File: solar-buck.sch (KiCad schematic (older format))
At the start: 52 parts, among them J1 PV_input, J2 Conn_02x19_Odd_Even, J3 Conn_02x19_Odd_Even, J4 Load_output, J5 Batt_output, J6 LED_ON, Q2 PMN30ENEA, Q3 NX3008PBK, Q4 NX3008PBK, SW1 SW_Push, SW2 SW_Push, SW3 SW_Push, SW4 SW_Push, U1 TS2937, U2 VN5E160MS-E, U3 MCP1804, U4 L6285E, U5 MAX4377

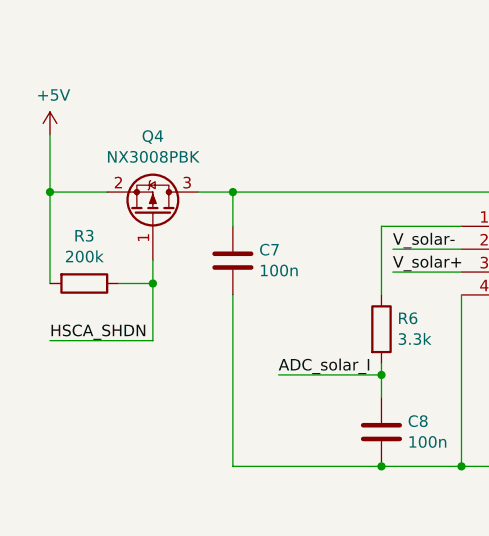
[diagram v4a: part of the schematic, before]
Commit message: Updated PCB footprints
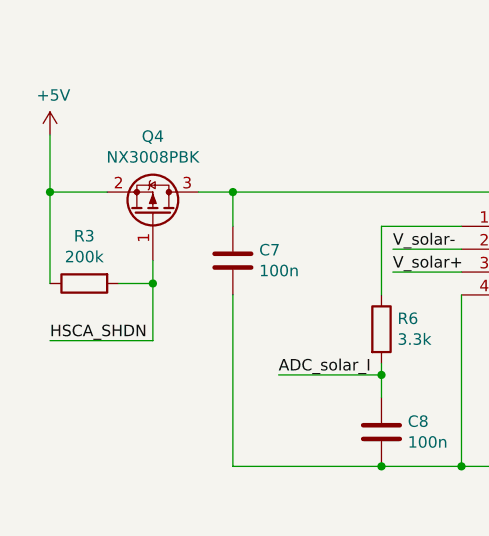
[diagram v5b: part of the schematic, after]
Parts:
- C10, C11, C2, C4, C5, C7, C8, C9: footprint Capacitor_SMD:C_0805_2012Metric_Pad1.15x1.40mm_HandSolder -> Capacitor_SMD:C_0603_1608Metric_Pad1.05x0.95mm_HandSolder
- C3: footprint Capacitor_SMD:CP_Elec_6.3x5.4 -> Capacitor_SMD:CP_Elec_6.3x7.7
- C6: footprint Capacitor_SMD:CP_Elec_5x5.4 -> Capacitor_SMD:CP_Elec_4x5.4
- R1, R10, R11, R12, R13, R14, R2, R3, R4, R5, R6, R7, R8, R9: footprint Resistor_SMD:R_0805_2012Metric_Pad1.15x1.40mm_HandSolder -> Resistor_SMD:R_0603_1608Metric_Pad1.05x0.95mm_HandSolder
- U2: footprint (none) -> Package_SO:SO-8_3.9x4.9mm_P1.27mm
- U5: footprint (none) -> Package_SO:MSOP-8_3x3mm_P0.65mm
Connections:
- net +5V: now also R3.1; no longer R3.2
- net HSCA_SHDN: now also R3.2; no longer R3.1
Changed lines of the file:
@@
 F 0 "C6" H 3918 4096 50  0000 L CNN
 F 1 "10u" H 3918 4005 50  0000 L CNN
-F 2 "Capacitor_SMD:CP_Elec_5x5.4" H 3838 3900 50  0001 C CNN
+F 2 "Capacitor_SMD:CP_Elec_4x5.4" H 3838 3900 50  0001 C CNN
 F 3 "~" H 3800 4050 50  0001 C CNN
 	1    3800 4050
@@
 F 0 "R2" H 10450 4650 50  0000 L CNN
 F 1 "100" H 10450 4550 50  0000 L CNN
-F 2 "Resistor_SMD:R_0805_2012Metric_Pad1.15x1.40mm_HandSolder" V 10330 4600 50  0001 C CNN
+F 2 "Resistor_SMD:R_0603_1608Metric_Pad1.05x0.95mm_HandSolder" V 10330 4600 50  0001 C CNN
 F 3 "~" H 10400 4600 50  0001 C CNN
 	1    10400 4600
@@
 F 0 "C4" H 2665 3696 50  0000 L CNN
 F 1 "100n" H 2665 3605 50  0000 L CNN
-F 2 "Capacitor_SMD:C_0805_2012Metric_Pad1.15x1.40mm_HandSolder" H 2588 3500 50  0001 C CNN
+F 2 "Capacitor_SMD:C_0603_1608Metric_Pad1.05x0.95mm_HandSolder" H 2588 3500 50  0001 C CNN
 F 3 "~" H 2550 3650 50  0001 C CNN
 	1    2550 3650
@@
 F 0 "C7" H 1765 6546 50  0000 L CNN
 F 1 "100n" H 1765 6455 50  0000 L CNN
-F 2 "Capacitor_SMD:C_0805_2012Metric_Pad1.15x1.40mm_HandSolder" H 1688 6350 50  0001 C CNN
+F 2 "Capacitor_SMD:C_0603_1608Metric_Pad1.05x0.95mm_HandSolder" H 1688 6350 50  0001 C CNN
 F 3 "~" H 1650 6500 50  0001 C CNN
 	1    1650 6500
@@
 F 0 "C5" H 915 4046 50  0000 L CNN
 F 1 "100n" H 915 3955 50  0000 L CNN
-F 2 "Capacitor_SMD:C_0805_2012Metric_Pad1.15x1.40mm_HandSolder" H 838 3850 50  0001 C CNN
+F 2 "Capacitor_SMD:C_0603_1608Metric_Pad1.05x0.95mm_HandSolder" H 838 3850 50  0001 C CNN
 F 3 "~" H 800 4000 50  0001 C CNN
 	1    800  4000
@@
 F 0 "R9" H 4780 7054 50  0000 R CNN
 F 1 "200k" H 4780 7145 50  0000 R CNN
-F 2 "Resistor_SMD:R_0805_2012Metric_Pad1.15x1.40mm_HandSolder" V 4780 7100 50  0001 C CNN
+F 2 "Resistor_SMD:R_0603_1608Metric_Pad1.05x0.95mm_HandSolder" V 4780 7100 50  0001 C CNN
 F 3 "~" H 4850 7100 50  0001 C CNN
 	1    4850 7100
@@
 F 0 "R4" H 4780 6604 50  0000 R CNN
 F 1 "1.8M" H 4780 6695 50  0000 R CNN
-F 2 "Resistor_SMD:R_0805_2012Metric_Pad1.15x1.40mm_HandSolder" V 4780 6650 50  0001 C CNN
+F 2 "Resistor_SMD:R_0603_1608Metric_Pad1.05x0.95mm_HandSolder" V 4780 6650 50  0001 C CNN
 F 3 "~" H 4850 6650 50  0001 C CNN
 	1    4850 6650
@@
 F 0 "R10" H 5830 7054 50  0000 R CNN
 F 1 "200k" H 5830 7145 50  0000 R CNN
-F 2 "Resistor_SMD:R_0805_2012Metric_Pad1.15x1.40mm_HandSolder" V 5830 7100 50  0001 C CNN
+F 2 "Resistor_SMD:R_0603_1608Metric_Pad1.05x0.95mm_HandSolder" V 5830 7100 50  0001 C CNN
 F 3 "~" H 5900 7100 50  0001 C CNN
 	1    5900 7100
@@
 F 0 "R5" H 5830 6604 50  0000 R CNN
 F 1 "1.8M" H 5830 6695 50  0000 R CNN
-F 2 "Resistor_SMD:R_0805_2012Metric_Pad1.15x1.40mm_HandSolder" V 5830 6650 50  0001 C CNN
+F 2 "Resistor_SMD:R_0603_1608Metric_Pad1.05x0.95mm_HandSolder" V 5830 6650 50  0001 C CNN
 F 3 "~" H 5900 6650 50  0001 C CNN
 	1    5900 6650
@@
 F 0 "R6" H 2370 6846 50  0000 L CNN
 F 1 "3.3k" H 2370 6755 50  0000 L CNN
-F 2 "Resistor_SMD:R_0805_2012Metric_Pad1.15x1.40mm_HandSolder" V 2230 6800 50  0001 C CNN
+F 2 "Resistor_SMD:R_0603_1608Metric_Pad1.05x0.95mm_HandSolder" V 2230 6800 50  0001 C CNN
 F 3 "~" H 2300 6800 50  0001 C CNN
 	1    2300 6800
@@
 F 0 "C10" H 3935 7204 50  0000 R CNN
 F 1 "100n" H 3935 7295 50  0000 R CNN
-F 2 "Capacitor_SMD:C_0805_2012Metric_Pad1.15x1.40mm_HandSolder" H 4088 7100 50  0001 C CNN
+F 2 "Capacitor_SMD:C_0603_1608Metric_Pad1.05x0.95mm_HandSolder" H 4088 7100 50  0001 C CNN
 F 3 "~" H 4050 7250 50  0001 C CNN
 	1    4050 7250
@@
 F 0 "C8" H 2415 7296 50  0000 L CNN
 F 1 "100n" H 2415 7205 50  0000 L CNN
-F 2 "Capacitor_SMD:C_0805_2012Metric_Pad1.15x1.40mm_HandSolder" H 2338 7100 50  0001 C CNN
+F 2 "Capacitor_SMD:C_0603_1608Metric_Pad1.05x0.95mm_HandSolder" H 2338 7100 50  0001 C CNN
 F 3 "~" H 2300 7250 50  0001 C CNN
 	1    2300 7250
@@
 F 0 "R8" H 3980 6804 50  0000 R CNN
 F 1 "3.3k" H 3980 6895 50  0000 R CNN
-F 2 "Resistor_SMD:R_0805_2012Metric_Pad1.15x1.40mm_HandSolder" V 3980 6850 50  0001 C CNN
+F 2 "Resistor_SMD:R_0603_1608Metric_Pad1.05x0.95mm_HandSolder" V 3980 6850 50  0001 C CNN
 F 3 "~" H 4050 6850 50  0001 C CNN
 	1    4050 6850
@@
 F 0 "C3" H 2468 2946 50  0000 L CNN
 F 1 "100u" H 2468 2855 50  0000 L CNN
-F 2 "Capacitor_SMD:CP_Elec_6.3x5.4" H 2388 2750 50  0001 C CNN
+F 2 "Capacitor_SMD:CP_Elec_6.3x7.7" H 2388 2750 50  0001 C CNN
 F 3 "~" H 2350 2900 50  0001 C CNN
 	1    2350 2900
@@
 F 0 "R3" V 793 6600 50  0000 C CNN
 F 1 "200k" V 884 6600 50  0000 C CNN
-F 2 "Resistor_SMD:R_0805_2012Metric_Pad1.15x1.40mm_HandSolder" V 930 6600 50  0001 C CNN
+F 2 "Resistor_SMD:R_0603_1608Metric_Pad1.05x0.95mm_HandSolder" V 930 6600 50  0001 C CNN
 F 3 "~" H 1000 6600 50  0001 C CNN
 	1    1000 6600
-	0    1    1    0
+	0    -1   1    0
 $EndComp
 Wire Wire Line
@@
 F 0 "R1" H 7770 4296 50  0000 L CNN
 F 1 "200k" H 7770 4205 50  0000 L CNN
-F 2 "Resistor_SMD:R_0805_2012Metric_Pad1.15x1.40mm_HandSolder" V 7630 4250 50  0001 C CNN
+F 2 "Resistor_SMD:R_0603_1608Metric_Pad1.05x0.95mm_HandSolder" V 7630 4250 50  0001 C CNN
 F 3 "~" H 7700 4250 50  0001 C CNN
 	1    7700 4250
@@
 F 0 "C2" H 4765 2746 50  0000 L CNN
 F 1 "1u" H 4765 2655 50  0000 L CNN
-F 2 "Capacitor_SMD:C_0805_2012Metric_Pad1.15x1.40mm_HandSolder" H 4688 2550 50  0001 C CNN
+F 2 "Capacitor_SMD:C_0603_1608Metric_Pad1.05x0.95mm_HandSolder" H 4688 2550 50  0001 C CNN
 F 3 "~" H 4650 2700 50  0001 C CNN
 	1    4650 2700
@@
 F 0 "U2" H 6500 3115 50  0000 C CNN
 F 1 "VN5E160MS-E" H 6500 3024 50  0000 C CNN
-F 2 "" H 6500 3350 50  0001 C CNN
+F 2 "Package_SO:SO-8_3.9x4.9mm_P1.27mm" H 6500 3350 50  0001 C CNN
 F 3 "" H 6500 3350 50  0001 C CNN
 	1    6500 2700
@@
 F 0 "U5" H 3150 6915 50  0000 C CNN
 F 1 "MAX4377" H 3150 6824 50  0000 C CNN
-F 2 "" H 3150 6550 50  0001 C CNN
+F 2 "Package_SO:MSOP-8_3x3mm_P0.65mm" H 3150 6550 50  0001 C CNN
 F 3 "" H 3150 6550 50  0001 C CNN
 	1    3150 6500
@@
 F 0 "R12" H 7050 2950 50  0000 L CNN
 F 1 "100" H 7050 2850 50  0000 L CNN
-F 2 "Resistor_SMD:R_0805_2012Metric_Pad1.15x1.40mm_HandSolder" V 6930 2900 50  0001 C CNN
+F 2 "Resistor_SMD:R_0603_1608Metric_Pad1.05x0.95mm_HandSolder" V 6930 2900 50  0001 C CNN
 F 3 "~" H 7000 2900 50  0001 C CNN
 	1    7000 2900
@@
 F 0 "R14" H 7050 3300 50  0000 L CNN
 F 1 "100" H 7050 3200 50  0000 L CNN
-F 2 "Resistor_SMD:R_0805_2012Metric_Pad1.15x1.40mm_HandSolder" V 6930 3250 50  0001 C CNN
+F 2 "Resistor_SMD:R_0603_1608Metric_Pad1.05x0.95mm_HandSolder" V 6930 3250 50  0001 C CNN
 F 3 "~" H 7000 3250 50  0001 C CNN
 	1    7000 3250
@@
 F 0 "R13" V 7507 3050 50  0000 C CNN
 F 1 "10k" V 7416 3050 50  0000 C CNN
-F 2 "Resistor_SMD:R_0805_2012Metric_Pad1.15x1.40mm_HandSolder" V 7230 3050 50  0001 C CNN
+F 2 "Resistor_SMD:R_0603_1608Metric_Pad1.05x0.95mm_HandSolder" V 7230 3050 50  0001 C CNN
 F 3 "~" H 7300 3050 50  0001 C CNN
 	1    7300 3050
@@
 F 0 "R7" V 7507 2550 50  0000 C CNN
 F 1 "10k" V 7416 2550 50  0000 C CNN
-F 2 "Resistor_SMD:R_0805_2012Metric_Pad1.15x1.40mm_HandSolder" V 7230 2550 50  0001 C CNN
+F 2 "Resistor_SMD:R_0603_1608Metric_Pad1.05x0.95mm_HandSolder" V 7230 2550 50  0001 C CNN
 F 3 "~" H 7300 2550 50  0001 C CNN
 	1    7300 2550
@@
 F 0 "R11" V 7257 2650 50  0000 C CNN
 F 1 "10k" V 7166 2650 50  0000 C CNN
-F 2 "Resistor_SMD:R_0805_2012Metric_Pad1.15x1.40mm_HandSolder" V 6980 2650 50  0001 C CNN
+F 2 "Resistor_SMD:R_0603_1608Metric_Pad1.05x0.95mm_HandSolder" V 6980 2650 50  0001 C CNN
 F 3 "~" H 7050 2650 50  0001 C CNN
 	1    7050 2650
@@
 F 0 "C9" H 5085 7054 50  0000 R CNN
 F 1 "100n" H 5085 7145 50  0000 R CNN
-F 2 "Capacitor_SMD:C_0805_2012Metric_Pad1.15x1.40mm_HandSolder" H 5238 6950 50  0001 C CNN
+F 2 "Capacitor_SMD:C_0603_1608Metric_Pad1.05x0.95mm_HandSolder" H 5238 6950 50  0001 C CNN
 F 3 "~" H 5200 7100 50  0001 C CNN
 	1    5200 7100
@@
 F 0 "C11" H 6185 7054 50  0000 R CNN
 F 1 "100n" H 6185 7145 50  0000 R CNN
-F 2 "Capacitor_SMD:C_0805_2012Metric_Pad1.15x1.40mm_HandSolder" H 6338 6950 50  0001 C CNN
+F 2 "Capacitor_SMD:C_0603_1608Metric_Pad1.05x0.95mm_HandSolder" H 6338 6950 50  0001 C CNN
 F 3 "~" H 6300 7100 50  0001 C CNN
 	1    6300 7100

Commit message: PCB complete
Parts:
- added TP1, TP10, TP11, TP12, TP2, TP3, TP4, TP5, TP6, TP7, TP8, TP9: TestPoint, TestPoint:TestPoint_Pad_1.5x1.5mm, symbol Connector:TestPoint
- U2, U4: footprint Package_SO:SO-8_3.9x4.9mm_P1.27mm -> Package_SO:SOIC-8_3.9x4.9mm_P1.27mm
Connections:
- net +5V: now also TP3.1
- net ADC_batt: now also R4.2, TP9.1; no longer R4.1
- net ADC_batt_I: now also TP12.1
- net ADC_solar: now also R5.2, TP10.1; no longer R5.1
- net ADC_solar_I: now also TP11.1
- net PWM_buck: now also TP6.1
- net V_batt: now also R4.1, TP7.1, TP8.1; no longer R4.2
- net V_load: now also TP5.1
- net V_solar: now also R5.1, TP1.1, TP2.1; no longer R5.2
- net at C5.1, U3.5 (VOUT), U4.3 (VCC): now also TP4.1
- net PM_LBO: no longer names the net of J2.27 (Pin_27)
- no-connect marks 53 -> 54
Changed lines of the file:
@@
 Wire Wire Line
 	5300 4050 5300 3800
-Text Label 2650 1800 0    50   ~ 0
-V_solar
 Text Label 5050 3800 2    50   ~ 0
 V_batt
-Text Label 5900 2750 2    50   ~ 0
+Text Label 5750 2750 2    50   ~ 0
 V_load
 $Comp
@@
 Wire Wire Line
 	2550 3800 2900 3800
-Wire Wire Line
-	1200 3600 900  3600
 $Comp
 L power:GND #PWR010
@@
 Text Label 8650 2200 2    50   ~ 0
 LOAD_EN
-Text Label 8650 2300 2    50   ~ 0
-PM_LBO
 Text Label 9350 1200 0    50   ~ 0
 E5V
@@
 	8650 2200 8750 2200
 Wire Wire Line
-	8750 2300 8650 2300
-Wire Wire Line
 	9350 2700 9250 2700
 Wire Wire Line
@@
 F 3 "~" H 4850 6650 50  0001 C CNN
 	1    4850 6650
-	-1   0    0    1
+	-1   0    0    -1
 $EndComp
 $Comp
@@
 F 3 "~" H 5900 6650 50  0001 C CNN
 	1    5900 6650
-	-1   0    0    1
+	-1   0    0    -1
 $EndComp
 $Comp
@@
 Wire Wire Line
 	4050 6700 4050 6450
-Wire Wire Line
-	2300 7000 1850 7000
 Connection ~ 2300 7000
 Wire Wire Line
 	2300 7000 2300 6950
-Wire Wire Line
-	3600 7050 4050 7050
 Connection ~ 4050 7050
 Wire Wire Line
@@
 F 0 "U4" H 1700 4065 50  0000 C CNN
 F 1 "L6285E" H 1700 3974 50  0000 C CNN
-F 2 "Package_SO:SO-8_3.9x4.9mm_P1.27mm" H 1700 3750 50  0001 C CNN
+F 2 "Package_SO:SOIC-8_3.9x4.9mm_P1.27mm" H 1700 3750 50  0001 C CNN
 F 3 "" H 1700 3750 50  0001 C CNN
 	1    1700 3650
@@
 Wire Wire Line
 	2350 2650 2350 2750
-Wire Wire Line
-	2900 1800 2900 2650
 Connection ~ 2350 2650
 Wire Wire Line
@@
 	3600 2400 3600 2550
 Wire Wire Line
-	3600 2550 3900 2550
+	3600 2550 3750 2550
 Wire Wire Line
 	9200 4050 10000 4050
@@
 $EndComp
 Wire Wire Line
-	1550 1800 2000 1800
-Wire Wire Line
-	2450 1850 2450 1800
-Connection ~ 2450 1800
-Wire Wire Line
-	2450 1800 2900 1800
+	1550 1800 1650 1800
 Wire Wire Line
 	2000 1850 2000 1800
 Connection ~ 2000 1800
-Wire Wire Line
-	2000 1800 2450 1800
 Wire Wire Line
 	2000 2050 2000 2200
@@
 Connection ~ 4750 3800
 Wire Wire Line
-	4750 3800 5300 3800
+	4750 3800 5100 3800
 Wire Wire Line
 	4300 4050 4300 4300
@@
 F 0 "U2" H 6500 3115 50  0000 C CNN
 F 1 "VN5E160MS-E" H 6500 3024 50  0000 C CNN
-F 2 "Package_SO:SO-8_3.9x4.9mm_P1.27mm" H 6500 3350 50  0001 C CNN
+F 2 "Package_SO:SOIC-8_3.9x4.9mm_P1.27mm" H 6500 3350 50  0001 C CNN
 F 3 "" H 6500 3350 50  0001 C CNN
 	1    6500 2700
@@
 	6100 2750 6100 3050
 Wire Wire Line
-	5900 2750 6100 2750
+	5750 2750 5850 2750
 Connection ~ 6100 2750
 Wire Wire Line
@@
 Wire Wire Line
 	5200 6850 5200 6950
+$Comp
+L Connector:TestPoint TP1
+U 1 1 5DC4BC41
+P 1650 1550
+F 0 "TP1" H 1708 1622 50  0000 L CNN
+F 1 "TestPoint" H 1708 1577 50  0001 L CNN
+F 2 "TestPoint:TestPoint_Pad_1.5x1.5mm" H 1850 1550 50  0001 C CNN
+F 3 "~" H 1850 1550 50  0001 C CNN
+	1    1650 1550
+	1    0    0    -1
+$EndComp
+Connection ~ 1650 1800
+Wire Wire Line
+	1650 1800 2000 1800
+Wire Wire Line
+	2900 1800 2900 2650
+Wire Wire Line
+	2000 1800 2450 1800
+Connection ~ 2450 1800
+Wire Wire Line
+	2450 1850 2450 1800
+Wire Wire Line
+	2450 1800 2900 1800
+Text Label 2600 1800 0    50   ~ 0
+V_solar
+Wire Wire Line
+	1650 1550 1650 1800
+$Comp
+L Connector:TestPoint TP2
+U 1 1 5DC6D51B
+P 2900 1550
+F 0 "TP2" H 2958 1622 50  0000 L CNN
+F 1 "TestPoint" H 2958 1577 50  0001 L CNN
+F 2 "TestPoint:TestPoint_Pad_1.5x1.5mm" H 3100 1550 50  0001 C CNN
+F 3 "~" H 3100 1550 50  0001 C CNN
+	1    2900 1550
+	1    0    0    -1
+$EndComp
+Wire Wire Line
+	2900 1550 2900 1800
+$Comp
+L Connector:TestPoint TP4
+U 1 1 5DC8982C
+P 800 2400
+F 0 "TP4" H 858 2472 50  0000 L CNN
+F 1 "TestPoint" H 858 2427 50  0001 L CNN
+F 2 "TestPoint:TestPoint_Pad_1.5x1.5mm" H 1000 2400 50  0001 C CNN
+F 3 "~" H 1000 2400 50  0001 C CNN
+	1    800  2400
+	1    0    0    -1
+$EndComp
+Wire Wire Line
+	800  2400 800  2650
+$Comp
+L Connector:TestPoint TP7
+U 1 1 5DC97846
+P 4300 3550
+F 0 "TP7" H 4358 3622 50  0000 L CNN
+F 1 "TestPoint" H 4358 3577 50  0001 L CNN
+F 2 "TestPoint:TestPoint_Pad_1.5x1.5mm" H 4500 3550 50  0001 C CNN
+F 3 "~" H 4500 3550 50  0001 C CNN
+	1    4300 3550
+	1    0    0    -1
+$EndComp
+Wire Wire Line
+	4300 3550 4300 3800
+$Comp
+L Connector:TestPoint TP8
+U 1 1 5DCA5AFB
+P 5100 3550
+F 0 "TP8" H 5158 3622 50  0000 L CNN
+F 1 "TestPoint" H 5158 3577 50  0001 L CNN
+F 2 "TestPoint:TestPoint_Pad_1.5x1.5mm" H 5300 3550 50  0001 C CNN
+F 3 "~" H 5300 3550 50  0001 C CNN
+	1    5100 3550
+	1    0    0    -1
+$EndComp
+Wire Wire Line
+	5100 3550 5100 3800
+$Comp
+L Connector:TestPoint TP3
+U 1 1 5DCB3DB1
+P 3750 2300
+F 0 "TP3" H 3808 2372 50  0000 L CNN
+F 1 "TestPoint" H 3808 2327 50  0001 L CNN
+F 2 "TestPoint:TestPoint_Pad_1.5x1.5mm" H 3950 2300 50  0001 C CNN
+F 3 "~" H 3950 2300 50  0001 C CNN
+	1    3750 2300
+	1    0    0    -1
+$EndComp
+Wire Wire Line
+	3750 2300 3750 2550
+$Comp
+L Connector:TestPoint TP5
+U 1 1 5DCC271C
+P 5850 2750
+F 0 "TP5" H 5908 2822 50  0000 L CNN
+F 1 "TestPoint" H 5908 2777 50  0001 L CNN
+F 2 "TestPoint:TestPoint_Pad_1.5x1.5mm" H 6050 2750 50  0001 C CNN
+F 3 "~" H 6050 2750 50  0001 C CNN
+	1    5850 2750
+	1    0    0    -1
+$EndComp
+Connection ~ 5850 2750
+Wire Wire Line
+	5850 2750 6100 2750
+$Comp
+L Connector:TestPoint TP11
+U 1 1 5DD0B8DE
+P 1800 6950
+F 0 "TP11" H 1858 7022 50  0000 L CNN
+F 1 "TestPoint" H 1858 6977 50  0001 L CNN
+F 2 "TestPoint:TestPoint_Pad_1.5x1.5mm" H 2000 6950 50  0001 C CNN
+F 3 "~" H 2000 6950 50  0001 C CNN
+	1    1800 6950
+	1    0    0    -1
+$EndComp
+$Comp
+L Connector:TestPoint TP12
+U 1 1 5DD37B09
+P 3550 7000
+F 0 "TP12" H 3608 7072 50  0000 L CNN
+F 1 "TestPoint" H 3608 7027 50  0001 L CNN
+F 2 "TestPoint:TestPoint_Pad_1.5x1.5mm" H 3750 7000 50  0001 C CNN
+F 3 "~" H 3750 7000 50  0001 C CNN
+	1    3550 7000
+	1    0    0    -1
+$EndComp
+$Comp
+L Connector:TestPoint TP9
+U 1 1 5DD37FC7
+P 5200 6850
+F 0 "TP9" H 5258 6922 50  0000 L CNN
+F 1 "TestPoint" H 5258 6877 50  0001 L CNN
+F 2 "TestPoint:TestPoint_Pad_1.5x1.5mm" H 5400 6850 50  0001 C CNN
+F 3 "~" H 5400 6850 50  0001 C CNN
+	1    5200 6850
+	1    0    0    -1
+$EndComp
+Connection ~ 5200 6850
+$Comp
+L Connector:TestPoint TP10
+U 1 1 5DD382CA
+P 6300 6850
+F 0 "TP10" H 6358 6922 50  0000 L CNN
+F 1 "TestPoint" H 6358 6877 50  0001 L CNN
+F 2 "TestPoint:TestPoint_Pad_1.5x1.5mm" H 6500 6850 50  0001 C CNN
+F 3 "~" H 6500 6850 50  0001 C CNN
+	1    6300 6850
+	1    0    0    -1
+$EndComp
+Connection ~ 6300 6850
+Wire Wire Line
+	3550 7000 3550 7050
+Wire Wire Line
+	3550 7050 4050 7050
+Wire Wire Line
+	1800 7000 1800 6950
+Wire Wire Line
+	1800 7000 2300 7000
+$Comp
+L Connector:TestPoint TP6
+U 1 1 5DD64B61
+P 850 3550
+F 0 "TP6" H 908 3622 50  0000 L CNN
+F 1 "TestPoint" H 908 3577 50  0001 L CNN
+F 2 "TestPoint:TestPoint_Pad_1.5x1.5mm" H 1050 3550 50  0001 C CNN
+F 3 "~" H 1050 3550 50  0001 C CNN
+	1    850  3550
+	1    0    0    -1
+$EndComp
+Wire Wire Line
+	850  3550 850  3600
+Wire Wire Line
+	850  3600 1200 3600
+Connection ~ 5100 3800
+Wire Wire Line
+	5100 3800 5300 3800
+Connection ~ 800  2650
+Connection ~ 2900 1800
+Connection ~ 3750 2550
+Wire Wire Line
+	3750 2550 3900 2550
+NoConn ~ 8750 2300
 $EndSCHEMATC

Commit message: Final changes
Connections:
- net V_batt: no longer TP7.1, TP8.1
- net V_batt+: now also TP7.1
- net V_batt-: now also TP8.1
- net V_solar: no longer TP1.1, TP2.1
- net V_solar+: now also TP1.1
- net V_solar-: now also TP2.1
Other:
- moved on the sheet: TP1, TP2, TP7, TP8
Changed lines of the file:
@@
 $EndComp
-Wire Wire Line
-	1550 1800 1650 1800
 Wire Wire Line
 	2000 1850 2000 1800
@@
 	4750 3850 4750 3800
 Connection ~ 4750 3800
-Wire Wire Line
-	4750 3800 5100 3800
 Wire Wire Line
 	4300 4050 4300 4300
@@
 L Connector:TestPoint TP1
 U 1 1 5DC4BC41
-P 1650 1550
-F 0 "TP1" H 1708 1622 50  0000 L CNN
-F 1 "TestPoint" H 1708 1577 50  0001 L CNN
-F 2 "TestPoint:TestPoint_Pad_1.5x1.5mm" H 1850 1550 50  0001 C CNN
-F 3 "~" H 1850 1550 50  0001 C CNN
-	1    1650 1550
-	1    0    0    -1
-$EndComp
-Connection ~ 1650 1800
-Wire Wire Line
-	1650 1800 2000 1800
+P 2000 2200
+F 0 "TP1" H 2058 2272 50  0000 L CNN
+F 1 "TestPoint" H 2058 2227 50  0001 L CNN
+F 2 "TestPoint:TestPoint_Pad_1.5x1.5mm" H 2200 2200 50  0001 C CNN
+F 3 "~" H 2200 2200 50  0001 C CNN
+	1    2000 2200
+	-1   0    0    1
+$EndComp
 Wire Wire Line
 	2900 1800 2900 2650
@@
 Text Label 2600 1800 0    50   ~ 0
 V_solar
-Wire Wire Line
-	1650 1550 1650 1800
 $Comp
 L Connector:TestPoint TP2
 U 1 1 5DC6D51B
-P 2900 1550
-F 0 "TP2" H 2958 1622 50  0000 L CNN
-F 1 "TestPoint" H 2958 1577 50  0001 L CNN
-F 2 "TestPoint:TestPoint_Pad_1.5x1.5mm" H 3100 1550 50  0001 C CNN
-F 3 "~" H 3100 1550 50  0001 C CNN
-	1    2900 1550
-	1    0    0    -1
-$EndComp
-Wire Wire Line
-	2900 1550 2900 1800
+P 2450 2200
+F 0 "TP2" H 2508 2272 50  0000 L CNN
+F 1 "TestPoint" H 2508 2227 50  0001 L CNN
+F 2 "TestPoint:TestPoint_Pad_1.5x1.5mm" H 2650 2200 50  0001 C CNN
+F 3 "~" H 2650 2200 50  0001 C CNN
+	1    2450 2200
+	-1   0    0    1
+$EndComp
 $Comp
 L Connector:TestPoint TP4
@@
 L Connector:TestPoint TP7
 U 1 1 5DC97846
-P 4300 3550
-F 0 "TP7" H 4358 3622 50  0000 L CNN
-F 1 "TestPoint" H 4358 3577 50  0001 L CNN
-F 2 "TestPoint:TestPoint_Pad_1.5x1.5mm" H 4500 3550 50  0001 C CNN
-F 3 "~" H 4500 3550 50  0001 C CNN
-	1    4300 3550
-	1    0    0    -1
-$EndComp
-Wire Wire Line
-	4300 3550 4300 3800
+P 4300 4300
+F 0 "TP7" V 4150 4372 50  0000 C CNN
+F 1 "TestPoint" H 4358 4327 50  0001 L CNN
+F 2 "TestPoint:TestPoint_Pad_1.5x1.5mm" H 4500 4300 50  0001 C CNN
+F 3 "~" H 4500 4300 50  0001 C CNN
+	1    4300 4300
+	0    -1   -1   0
+$EndComp
 $Comp
 L Connector:TestPoint TP8
 U 1 1 5DCA5AFB
-P 5100 3550
-F 0 "TP8" H 5158 3622 50  0000 L CNN
-F 1 "TestPoint" H 5158 3577 50  0001 L CNN
-F 2 "TestPoint:TestPoint_Pad_1.5x1.5mm" H 5300 3550 50  0001 C CNN
-F 3 "~" H 5300 3550 50  0001 C CNN
-	1    5100 3550
-	1    0    0    -1
-$EndComp
-Wire Wire Line
-	5100 3550 5100 3800
+P 5050 4300
+F 0 "TP8" H 4992 4372 50  0000 R CNN
+F 1 "TestPoint" H 5108 4327 50  0001 L CNN
+F 2 "TestPoint:TestPoint_Pad_1.5x1.5mm" H 5250 4300 50  0001 C CNN
+F 3 "~" H 5250 4300 50  0001 C CNN
+	1    5050 4300
+	-1   0    0    -1
+$EndComp
 $Comp
 L Connector:TestPoint TP3
@@
 Wire Wire Line
 	850  3600 1200 3600
-Connection ~ 5100 3800
-Wire Wire Line
-	5100 3800 5300 3800
 Connection ~ 800  2650
-Connection ~ 2900 1800
 Connection ~ 3750 2550
 Wire Wire Line
 	3750 2550 3900 2550
 NoConn ~ 8750 2300
+Wire Wire Line
+	1550 1800 2000 1800
+Connection ~ 2000 2200
+Connection ~ 2450 2200
+Wire Wire Line
+	4750 3800 5300 3800
+Connection ~ 4300 4300
 $EndSCHEMATC
